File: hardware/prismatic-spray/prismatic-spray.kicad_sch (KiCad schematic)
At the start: 10 parts, among them J1 Conn_01x03_Male, J2 Conn_01x03_Male, SW1 SW_Push, SW2 SW_Push, SW3 SW_Push, U1 Pico

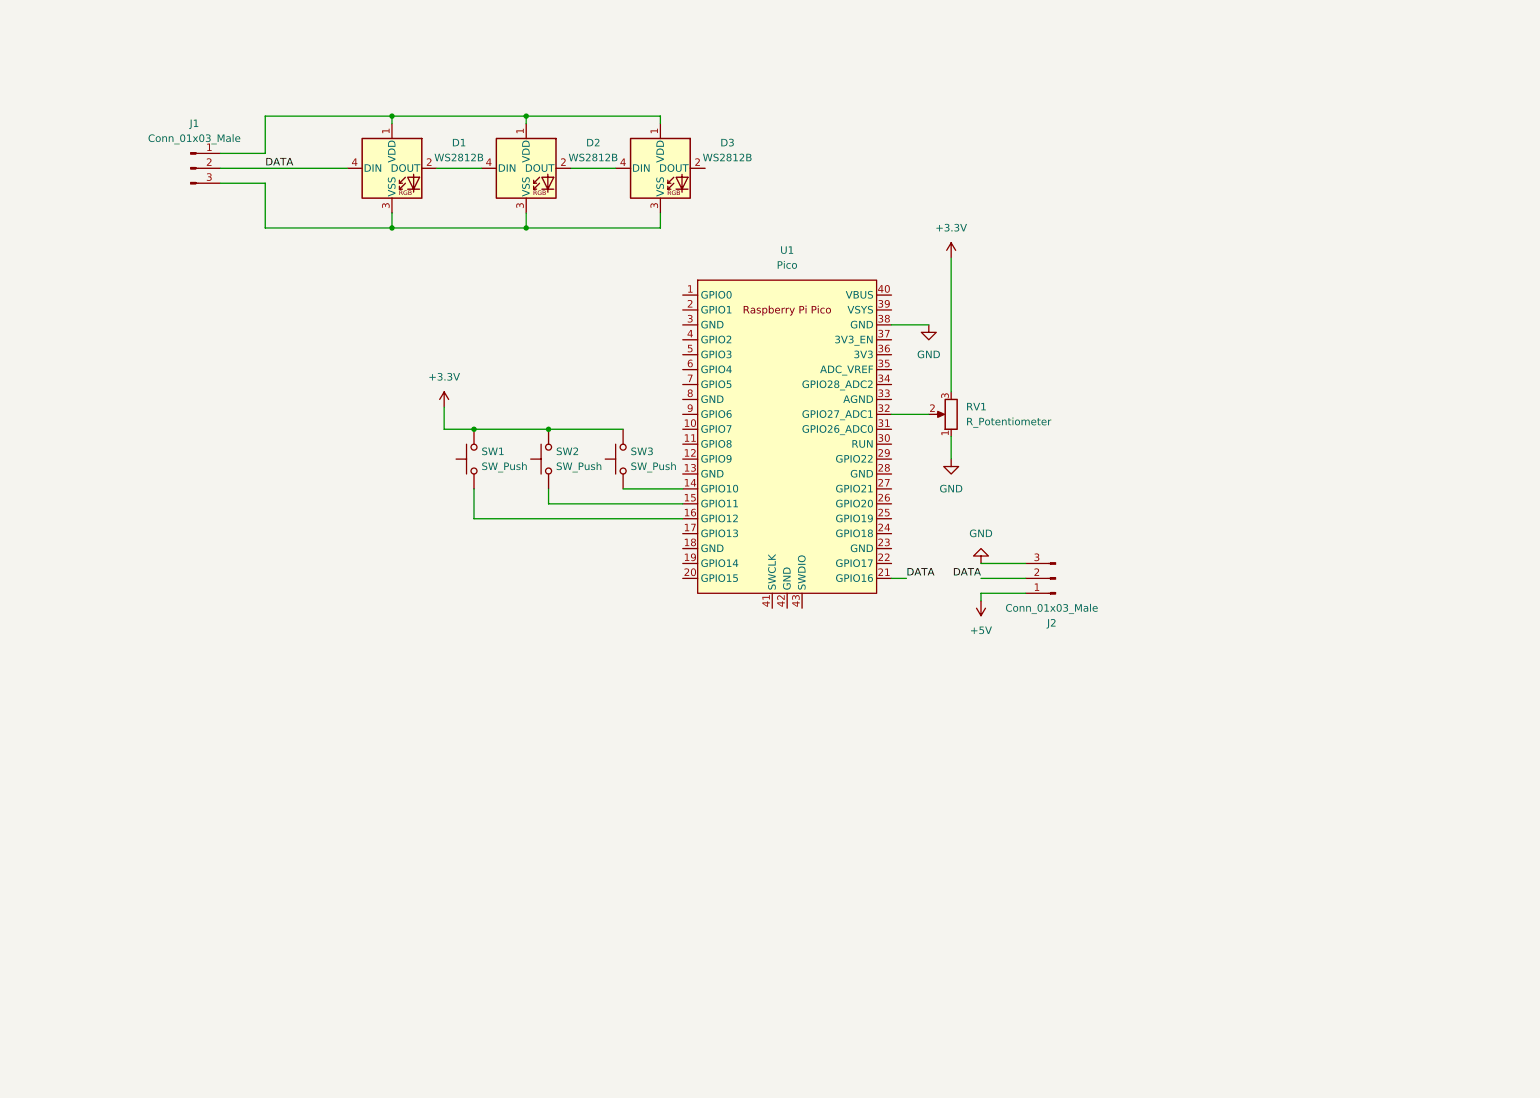
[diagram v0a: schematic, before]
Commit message: Add 4th button and LED
Also add a rotary encoder for color control (pot is for brightness)
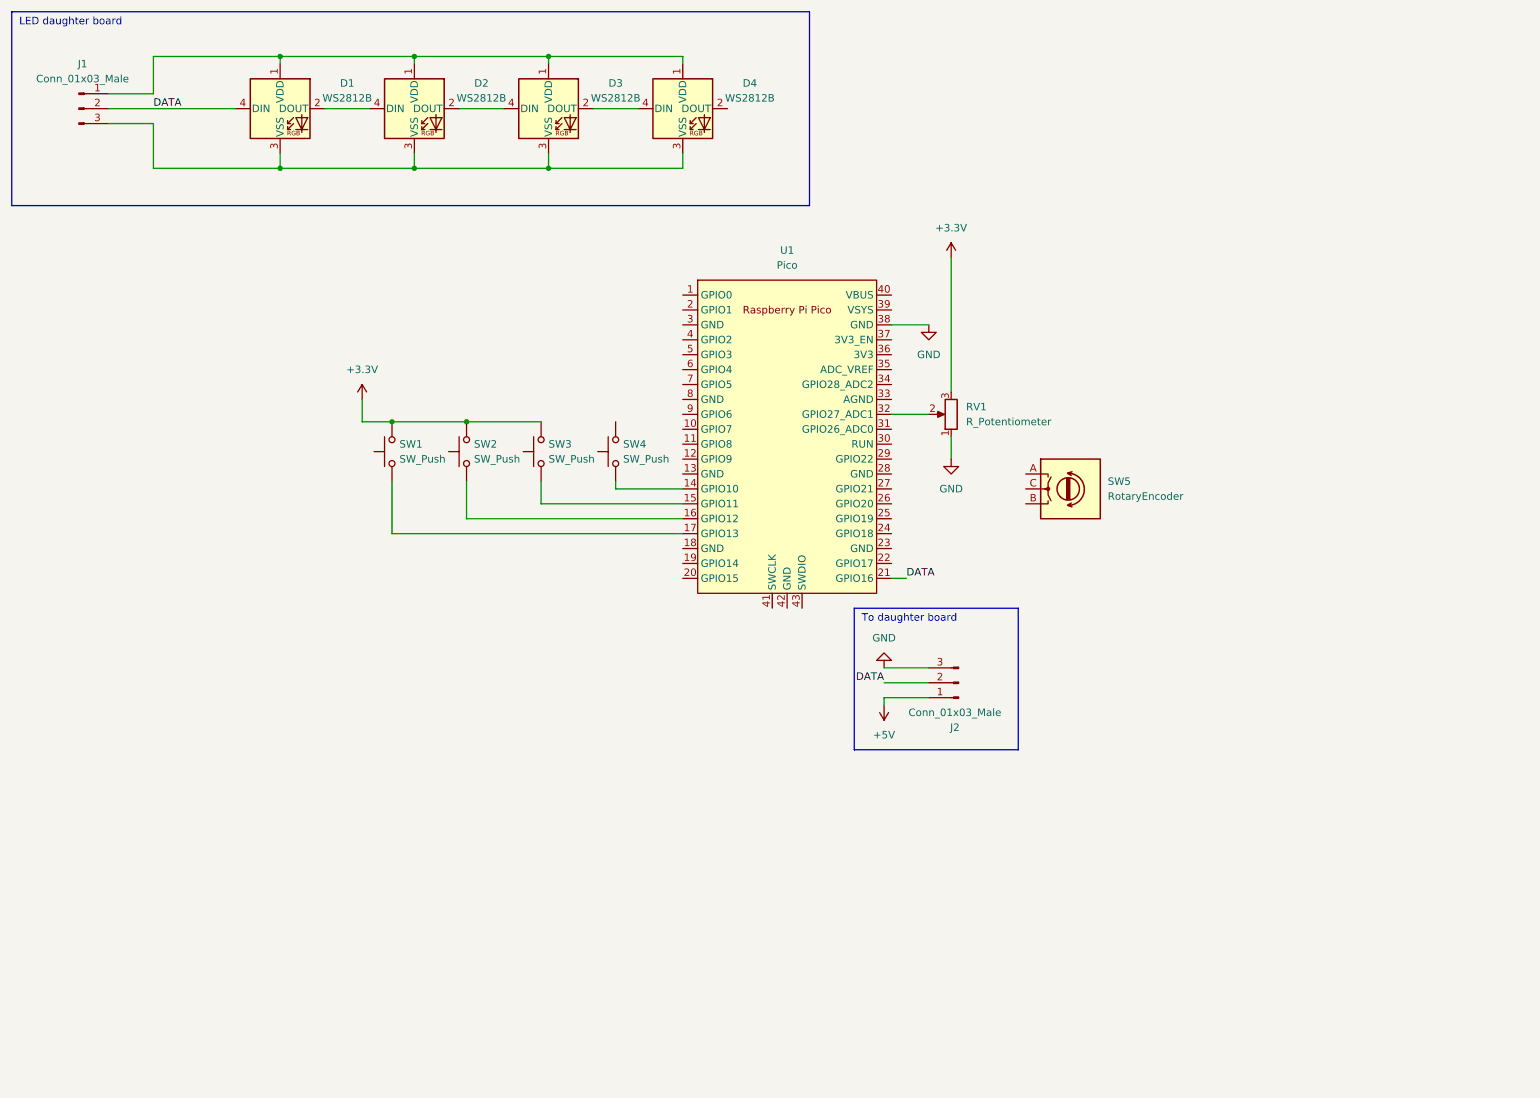
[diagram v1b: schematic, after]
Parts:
- added D4: WS2812B, LED_SMD:LED_WS2812B_PLCC4_5.0x5.0mm_P3.2mm, symbol LED:WS2812B
- added SW4: SW_Push, Button_Switch_Keyboard:SW_Cherry_MX_1.00u_PCB, symbol Switch:SW_Push
- added SW5: RotaryEncoder, symbol Device:RotaryEncoder
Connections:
- net at U1.14 (GPIO10): now also SW4.1; no longer SW3.1
- net at U1.15 (GPIO11): now also SW3.1; no longer SW2.1
- net at U1.16 (GPIO12): now also SW2.1; no longer SW1.1
- net at U1.17 (GPIO13): now also SW1.1
- net at D1.1 (VDD), D2.1 (VDD), D3.1 (VDD)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: now also D4.1 (VDD)
- net at D1.3 (VSS), D2.3 (VSS), D3.3 (VSS)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: now also D4.3 (VSS)
- net at D3.2 (DOUT): now also D4.4 (DIN)
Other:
- note added: "LED daughter board"
- note added: "To daughter board"
- moved on the sheet: D1, D2, D3, J1, J2, SW1, SW2, SW3

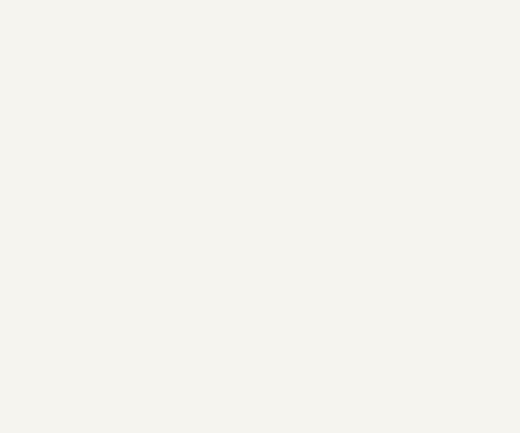
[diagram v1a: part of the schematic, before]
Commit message: Add mounting holes
- Add non-plated mounting holes
- Reposition board
- Place potentiometer
- TODO: rotary encoder
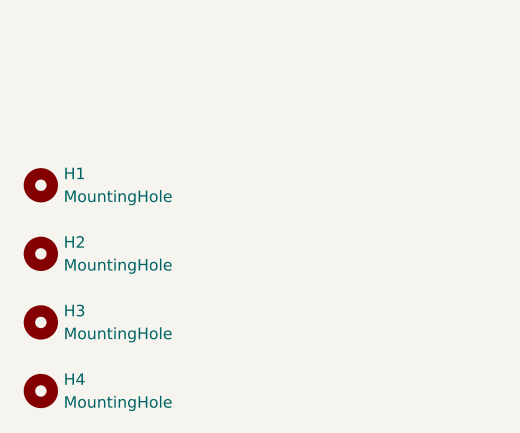
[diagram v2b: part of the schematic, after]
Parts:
- added H1, H2, H3, H4: MountingHole, MountingHole:MountingHole_2.7mm_M2.5, symbol Mechanical:MountingHole
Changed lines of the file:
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@@
     (pin "2")
+  )
+  (symbol (lib_id "Mechanical:MountingHole") (at 15.24 185.42 0) (unit 1)
+    (in_bom yes) (on_board yes) (fields_autoplaced)
+    (property "Reference" "H3" (id 0) (at 17.78 184.1499 0)
+      (effects (font (size 1.27 1.27)) (justify left))
+    )
+    (property "Value" "MountingHole" (id 1) (at 17.78 186.6899 0)
+      (effects (font (size 1.27 1.27)) (justify left))
+    )
+    (property "Footprint" "MountingHole:MountingHole_2.7mm_M2.5" (id 2) (at 15.24 185.42 0)
+      (effects (font (size 1.27 1.27)) hide)
+    )
+    (property "Datasheet" "~" (id 3) (at 15.24 185.42 0)
+      (effects (font (size 1.27 1.27)) hide)
+    )
   )
   (symbol (lib_id "Connector:Conn_01x03_Male") (at 173.99 127 180) (unit 1)
@@
     (pin "4")
   )
+  (symbol (lib_id "Mechanical:MountingHole") (at 15.24 193.04 0) (unit 1)
+    (in_bom yes) (on_board yes) (fields_autoplaced)
+    (property "Reference" "H4" (id 0) (at 17.78 191.7699 0)
+      (effects (font (size 1.27 1.27)) (justify left))
+    )
+    (property "Value" "MountingHole" (id 1) (at 17.78 194.3099 0)
+      (effects (font (size 1.27 1.27)) (justify left))
+    )
+    (property "Footprint" "MountingHole:MountingHole_2.7mm_M2.5" (id 2) (at 15.24 193.04 0)
+      (effects (font (size 1.27 1.27)) hide)
+    )
+    (property "Datasheet" "~" (id 3) (at 15.24 193.04 0)
+      (effects (font (size 1.27 1.27)) hide)
+    )
+  )
   (symbol (lib_id "power:+3.3V") (at 72.39 78.74 0) (unit 1)
     (in_bom yes) (on_board yes) (fields_autoplaced)
@@
     (pin "2")
   )
+  (symbol (lib_id "Mechanical:MountingHole") (at 15.24 177.8 0) (unit 1)
+    (in_bom yes) (on_board yes) (fields_autoplaced)
+    (property "Reference" "H2" (id 0) (at 17.78 176.5299 0)
+      (effects (font (size 1.27 1.27)) (justify left))
+    )
+    (property "Value" "MountingHole" (id 1) (at 17.78 179.0699 0)
+      (effects (font (size 1.27 1.27)) (justify left))
+    )
+    (property "Footprint" "MountingHole:MountingHole_2.7mm_M2.5" (id 2) (at 15.24 177.8 0)
+      (effects (font (size 1.27 1.27)) hide)
+    )
+    (property "Datasheet" "~" (id 3) (at 15.24 177.8 0)
+      (effects (font (size 1.27 1.27)) hide)
+    )
+  )
   (symbol (lib_id "Device:R_Potentiometer") (at 172.72 81.28 180) (unit 1)
     (in_bom yes) (on_board yes) (fields_autoplaced)
@@
     (pin "1")
     (pin "2")
+  )
+  (symbol (lib_id "Mechanical:MountingHole") (at 15.24 170.18 0) (unit 1)
+    (in_bom yes) (on_board yes) (fields_autoplaced)
+    (property "Reference" "H1" (id 0) (at 17.78 168.9099 0)
+      (effects (font (size 1.27 1.27)) (justify left))
+    )
+    (property "Value" "MountingHole" (id 1) (at 17.78 171.4499 0)
+      (effects (font (size 1.27 1.27)) (justify left))
+    )
+    (property "Footprint" "MountingHole:MountingHole_2.7mm_M2.5" (id 2) (at 15.24 170.18 0)
+      (effects (font (size 1.27 1.27)) hide)
+    )
+    (property "Datasheet" "~" (id 3) (at 15.24 170.18 0)
+      (effects (font (size 1.27 1.27)) hide)
+    )
   )
   (symbol (lib_id "LED:WS2812B") (at 127 29.21 0) (unit 1)
@@
       (reference "D4") (unit 1) (value "WS2812B") (footprint "LED_SMD:LED_WS2812B_PLCC4_5.0x5.0mm_P3.2mm")
     )
+    (path "/b853d9ac-7829-468f-99ac-dc9996502e94"
+      (reference "H1") (unit 1) (value "MountingHole") (footprint "MountingHole:MountingHole_2.7mm_M2.5")
+    )
+    (path "/a3d9e0bf-98f1-4a23-b70b-146421eebf6c"
+      (reference "H2") (unit 1) (value "MountingHole") (footprint "MountingHole:MountingHole_2.7mm_M2.5")
+    )
+    (path "/28ef2877-5844-4c5b-aa51-ed11ac9cc260"
+      (reference "H3") (unit 1) (value "MountingHole") (footprint "MountingHole:MountingHole_2.7mm_M2.5")
+    )
+    (path "/75a11b59-583e-4a99-95e9-5981e1dd9b99"
+      (reference "H4") (unit 1) (value "MountingHole") (footprint "MountingHole:MountingHole_2.7mm_M2.5")
+    )
     (path "/be4d27dd-53dc-40d1-9f15-e85a94ce57a3"

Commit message: Populate board with more footprints/3d models
- Add Cherry MX key switch 3d model
- Add PEC11 rotary encoder 3d model
- Add Raspberry Pi Pico 3d model
- Add PEC11 footprint (from schematic)
- Change rotary encoder schematic symbol to 3 encoder pins + 2 switch pins
- Add PCB rendering for docs
- Add image to local directory
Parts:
- removed SW5: RotaryEncoder, symbol Device:RotaryEncoder
- added SW5: RotaryEncoder_Switch, Footprints:pec11_rotary_encoder, symbol Device:RotaryEncoder_Switch
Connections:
- net +3V3: now also SW4.2, SW5.S1
- net at U1.4 (GPIO2): now also SW5.S2
- net at U1.5 (GPIO3): now also SW5.B
- net at U1.6 (GPIO4): now also SW5.C
- net at U1.7 (GPIO5): now also SW5.A
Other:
- note added: "1"
- note added: "2022-08-03"
- note added: "Prismatic Spray"
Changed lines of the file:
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@@
   (junction (at 90.17 82.55) (diameter 0) (color 0 0 0 0)
   )
+  (junction (at 102.87 82.55) (diameter 0) (color 0 0 0 0)
+  )
   (junction (at 58.42 39.37) (diameter 0) (color 0 0 0 0)
   )
@@
     (stroke (width 0) (type default) (color 0 0 0 0))
   )
+  (wire (pts (xy 97.79 55.88) (xy 72.39 55.88))
+    (stroke (width 0) (type default) (color 0 0 0 0))
+  )
+  (wire (pts (xy 100.33 71.12) (xy 100.33 73.66))
+    (stroke (width 0) (type default) (color 0 0 0 0))
+  )
+  (wire (pts (xy 97.79 71.12) (xy 97.79 76.2))
+    (stroke (width 0) (type default) (color 0 0 0 0))
+  )
   (wire (pts (xy 72.39 82.55) (xy 77.47 82.55))
     (stroke (width 0) (type default) (color 0 0 0 0))
@@
     (stroke (width 0) (type default) (color 0 0 0 0))
   )
+  (wire (pts (xy 72.39 55.88) (xy 72.39 54.61))
+    (stroke (width 0) (type default) (color 0 0 0 0))
+  )
   (wire (pts (xy 58.42 20.32) (xy 58.42 21.59))
     (stroke (width 0) (type default) (color 0 0 0 0))
@@
     (stroke (width 0) (type default) (color 0 0 0 0))
   )
+  (wire (pts (xy 115.57 55.88) (xy 115.57 68.58))
+    (stroke (width 0) (type default) (color 0 0 0 0))
+  )
   (wire (pts (xy 81.28 21.59) (xy 81.28 20.32))
     (stroke (width 0) (type default) (color 0 0 0 0))
@@
     (stroke (width 0) (type default) (color 0 0 0 0))
   )
+  (wire (pts (xy 127 68.58) (xy 115.57 68.58))
+    (stroke (width 0) (type default) (color 0 0 0 0))
+  )
+  (wire (pts (xy 172.72 54.61) (xy 172.72 77.47))
+    (stroke (width 0) (type default) (color 0 0 0 0))
+  )
   (wire (pts (xy 127 36.83) (xy 127 39.37))
     (stroke (width 0) (type default) (color 0 0 0 0))
@@
     (stroke (width 0) (type default) (color 0 0 0 0))
   )
+  (wire (pts (xy 100.33 73.66) (xy 127 73.66))
+    (stroke (width 0) (type default) (color 0 0 0 0))
+  )
+  (wire (pts (xy 97.79 76.2) (xy 127 76.2))
+    (stroke (width 0) (type default) (color 0 0 0 0))
+  )
   (polyline (pts (xy 156.21 114.3) (xy 184.15 114.3))
     (stroke (width 0) (type default) (color 0 0 0 0))
@@
     (stroke (width 0) (type default) (color 0 0 0 0))
   )
+  (wire (pts (xy 102.87 71.12) (xy 127 71.12))
+    (stroke (width 0) (type default) (color 0 0 0 0))
+  )
   (wire (pts (xy 127 101.6) (xy 77.47 101.6))
     (stroke (width 0) (type default) (color 0 0 0 0))
   )
+  (wire (pts (xy 102.87 55.88) (xy 115.57 55.88))
+    (stroke (width 0) (type default) (color 0 0 0 0))
+  )
   (wire (pts (xy 162.56 66.04) (xy 168.91 66.04))
     (stroke (width 0) (type default) (color 0 0 0 0))
@@
     (stroke (width 0) (type default) (color 0 0 0 0))
   )
-  (wire (pts (xy 172.72 54.61) (xy 172.72 77.47))
-    (stroke (width 0) (type default) (color 0 0 0 0))
-  )
   (wire (pts (xy 72.39 78.74) (xy 72.39 82.55))
     (stroke (width 0) (type default) (color 0 0 0 0))
   )
   (wire (pts (xy 161.29 129.54) (xy 161.29 130.81))
+    (stroke (width 0) (type default) (color 0 0 0 0))
+  )
+  (wire (pts (xy 102.87 82.55) (xy 115.57 82.55))
     (stroke (width 0) (type default) (color 0 0 0 0))
   )
@@
     (effects (font (size 1.27 1.27)) (justify left bottom))
   )
+  (text "1" (at 269.24 194.31 0)
+    (effects (font (size 1.27 1.27)) (justify left bottom))
+  )
   (text "To daughter board" (at 157.48 116.84 0)
     (effects (font (size 1.27 1.27)) (justify left bottom))
   )
+  (text "1" (at 187.96 184.15 0)
+    (effects (font (size 1.27 1.27)) (justify left bottom))
+  )
+  (text "2022-08-03" (at 207.01 194.31 0)
+    (effects (font (size 1.27 1.27)) (justify left bottom))
+  )
+  (text "1" (at 185.42 184.15 0)
+    (effects (font (size 1.27 1.27)) (justify left bottom))
+  )
+  (text "Prismatic Spray" (at 186.69 191.77 0)
+    (effects (font (size 2.54 2.54)) (justify left bottom))
+  )
   (label "DATA" (at 36.83 29.21 0)
     (effects (font (size 1.27 1.27)) (justify left bottom))
@@
     (pin "1")
   )
+  (symbol (lib_id "power:+3.3V") (at 72.39 54.61 0) (unit 1)
+    (in_bom yes) (on_board yes) (fields_autoplaced)
+    (property "Reference" "#PWR0107" (id 0) (at 72.39 58.42 0)
+      (effects (font (size 1.27 1.27)) hide)
+    )
+    (property "Value" "+3.3V" (id 1) (at 72.39 49.53 0))
+    (property "Footprint" "" (id 2) (at 72.39 54.61 0)
+      (effects (font (size 1.27 1.27)) hide)
+    )
+    (property "Datasheet" "" (id 3) (at 72.39 54.61 0)
+      (effects (font (size 1.27 1.27)) hide)
+    )
+    (pin "1")
+  )
   (symbol (lib_id "Switch:SW_Push") (at 115.57 87.63 90) (unit 1)
     (in_bom yes) (on_board yes) (fields_autoplaced)
@@
       (effects (font (size 1.27 1.27)) hide)
     )
+  )
+  (symbol (lib_id "Device:RotaryEncoder_Switch") (at 100.33 63.5 90) (unit 1)
+    (in_bom yes) (on_board yes)
+    (property "Reference" "SW5" (id 0) (at 90.17 60.96 90)
+      (effects (font (size 1.27 1.27)) (justify right))
+    )
+    (property "Value" "RotaryEncoder_Switch" (id 1) (at 73.66 63.5 90)
+      (effects (font (size 1.27 1.27)) (justify right))
+    )
+    (property "Footprint" "Footprints:pec11_rotary_encoder" (id 2) (at 96.266 67.31 0)
+      (effects (font (size 1.27 1.27)) hide)
+    )
+    (property "Datasheet" "https://cdn-shop.adafruit.com/datasheets/pec11.pdf" (id 3) (at 93.726 63.5 0)
+      (effects (font (size 1.27 1.27)) hide)
+    )
+    (pin "A")
+    (pin "B")
+    (pin "C")
+    (pin "S1")
+    (pin "S2")
   )
   (symbol (lib_id "Connector:Conn_01x03_Male") (at 173.99 127 180) (unit 1)
@@
     (pin "1")
   )
-  (symbol (lib_id "Device:RotaryEncoder") (at 193.04 93.98 0) (unit 1)
-    (in_bom yes) (on_board yes) (fields_autoplaced)
-    (property "Reference" "SW5" (id 0) (at 199.39 92.7099 0)
-      (effects (font (size 1.27 1.27)) (justify left))
-    )
-    (property "Value" "RotaryEncoder" (id 1) (at 199.39 95.2499 0)
-      (effects (font (size 1.27 1.27)) (justify left))
-    )
-    (property "Footprint" "" (id 2) (at 189.23 89.916 0)
-      (effects (font (size 1.27 1.27)) hide)
-    )
-    (property "Datasheet" "~" (id 3) (at 193.04 87.376 0)
-      (effects (font (size 1.27 1.27)) hide)
-    )
-    (pin "A")
-    (pin "B")
-    (pin "C")
-  )
   (sheet_instances
     (path "/" (page "1"))
@@
       (reference "#PWR0106") (unit 1) (value "+5V") (footprint "")
     )
+    (path "/08a4d803-0e5b-4631-a69f-cd1453cb8698"
+      (reference "#PWR0107") (unit 1) (value "+3.3V") (footprint "")
+    )
     (path "/68011628-52c2-40cd-8370-be8c41f48734"
       (reference "D1") (unit 1) (value "WS2812B") (footprint "LED_SMD:LED_WS2812B_PLCC4_5.0x5.0mm_P3.2mm")
@@
       (reference "SW4") (unit 1) (value "SW_Push") (footprint "Button_Switch_Keyboard:SW_Cherry_MX_1.00u_PCB")
     )
-    (path "/f7248c3f-4430-462b-ae79-b5c32fdcf0b6"
-      (reference "SW5") (unit 1) (value "RotaryEncoder") (footprint "")
+    (path "/361f552e-b3b5-4c1d-86d6-43d53614453f"
+      (reference "SW5") (unit 1) (value "RotaryEncoder_Switch") (footprint "Footprints:pec11_rotary_encoder")
     )
     (path "/618dd691-b311-4f9c-9908-ae7fda2219f2"

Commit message: Add P160 Potentiometer
- Add custom footprint
- TODO: add outline/screenprint for PCB size
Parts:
- RV1: footprint Potentiometer_THT:Potentiometer_ACP_CA6-H2,5_Horizontal -> Footprints:p160_potentiometer
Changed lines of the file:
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@@
       (effects (font (size 1.27 1.27)) (justify right))
     )
-    (property "Footprint" "Potentiometer_THT:Potentiometer_ACP_CA6-H2,5_Horizontal" (id 2) (at 172.72 81.28 0)
+    (property "Footprint" "Footprints:p160_potentiometer" (id 2) (at 172.72 81.28 0)
       (effects (font (size 1.27 1.27)) hide)
     )
@@
     )
     (path "/a68e407d-6968-4aa7-87a0-1d07ad018cf1"
-      (reference "RV1") (unit 1) (value "R_Potentiometer") (footprint "Potentiometer_THT:Potentiometer_ACP_CA6-H2,5_Horizontal")
+      (reference "RV1") (unit 1) (value "R_Potentiometer") (footprint "Footprints:p160_potentiometer")
     )
     (path "/a293ebe0-b0f7-4a89-b394-4a5c694aa469"
